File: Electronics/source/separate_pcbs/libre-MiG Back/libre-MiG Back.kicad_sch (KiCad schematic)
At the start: 7 parts, among them J17 Conn_01x06, J18 Conn_01x03, SW18 SKRHABE010, SW2 SW_Push, SW3 SW_Push

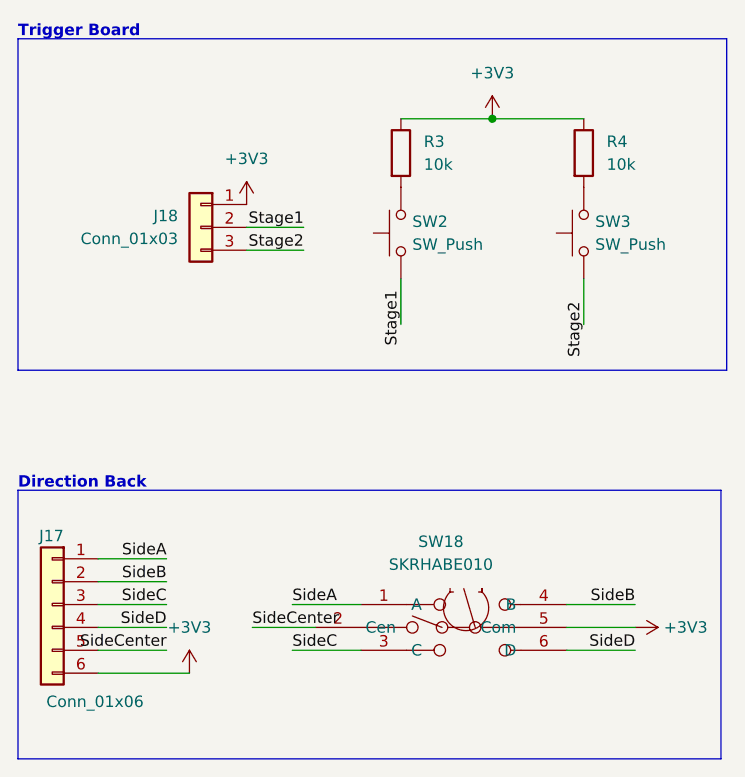
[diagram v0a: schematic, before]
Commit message: started layout and finished board shapes
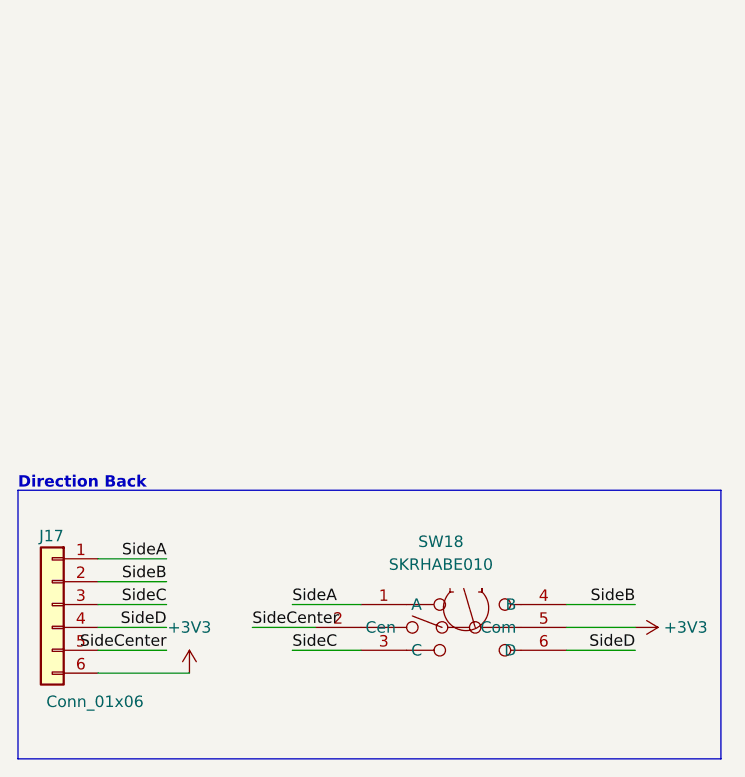
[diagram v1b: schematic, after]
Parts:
- removed J18: Conn_01x03, Connector_JST:JST_PH_S3B-PH-K_1x03_P2.00mm_Horizontal, symbol Connector_Generic:Conn_01x03
- removed R3, R4: 10k, Resistor_SMD:R_0805_2012Metric, symbol Device:R
- removed SW2, SW3: SW_Push, Button_Switch_THT:SW_PUSH-12mm_Wuerth-430476085716, symbol Switch:SW_Push
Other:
- note removed: "Trigger Board"
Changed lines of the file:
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@@
     (rev "v0.1")
-  )
-  (junction (at 111.76 57.15) (diameter 0) (color 0 0 0 0)
   )
   (wire (pts (xy 120.015 111.125) (xy 127.635 111.125))
@@
   )
   (wire (pts (xy 120.015 116.205) (xy 127.635 116.205))
-    (stroke (width 0) (type default) (color 0 0 0 0))
-  )
-  (wire (pts (xy 90.805 69.215) (xy 84.455 69.215))
     (stroke (width 0) (type default) (color 0 0 0 0))
   )
@@
     (stroke (width 0) (type default) (color 0 0 0 0))
   )
-  (polyline (pts (xy 59.055 48.26) (xy 137.795 48.26))
-    (stroke (width 0) (type default) (color 0 0 0 0))
-  )
-  (wire (pts (xy 90.805 71.755) (xy 84.455 71.755))
-    (stroke (width 0) (type default) (color 0 0 0 0))
-  )
-  (polyline (pts (xy 59.055 48.26) (xy 59.055 85.09))
-    (stroke (width 0) (type default) (color 0 0 0 0))
-  )
   (wire (pts (xy 75.565 108.585) (xy 67.945 108.585))
     (stroke (width 0) (type default) (color 0 0 0 0))
   )
-  (polyline (pts (xy 137.795 85.09) (xy 59.055 85.09))
-    (stroke (width 0) (type default) (color 0 0 0 0))
-  )
   (polyline (pts (xy 59.055 98.425) (xy 59.055 128.27))
-    (stroke (width 0) (type default) (color 0 0 0 0))
-  )
-  (wire (pts (xy 101.6 57.15) (xy 111.76 57.15))
-    (stroke (width 0) (type default) (color 0 0 0 0))
-  )
-  (wire (pts (xy 121.92 74.93) (xy 121.92 80.01))
-    (stroke (width 0) (type default) (color 0 0 0 0))
-  )
-  (polyline (pts (xy 137.795 48.26) (xy 137.795 85.09))
     (stroke (width 0) (type default) (color 0 0 0 0))
   )
@@
   )
   (wire (pts (xy 89.535 111.125) (xy 97.155 111.125))
-    (stroke (width 0) (type default) (color 0 0 0 0))
-  )
-  (wire (pts (xy 101.6 74.93) (xy 101.6 80.01))
     (stroke (width 0) (type default) (color 0 0 0 0))
   )
@@
     (stroke (width 0) (type default) (color 0 0 0 0))
   )
-  (wire (pts (xy 121.92 57.15) (xy 111.76 57.15))
-    (stroke (width 0) (type default) (color 0 0 0 0))
-  )
-  (text "Trigger Board" (at 59.055 48.26 0)
-    (effects (font (size 1.27 1.27) (thickness 0.254) bold) (justify left bottom))
-  )
   (text "Direction Back" (at 59.055 98.425 0)
     (effects (font (size 1.27 1.27) (thickness 0.254) bold) (justify left bottom))
   )
-  (label "Stage1" (at 101.6 76.2 270)
-    (effects (font (size 1.27 1.27)) (justify right bottom))
-  )
   (label "SideCenter" (at 75.565 116.205 180)
-    (effects (font (size 1.27 1.27)) (justify right bottom))
-  )
-  (label "Stage2" (at 90.805 71.755 180)
     (effects (font (size 1.27 1.27)) (justify right bottom))
   )
@@
     (effects (font (size 1.27 1.27)) (justify right bottom))
   )
-  (label "Stage2" (at 121.92 77.47 270)
-    (effects (font (size 1.27 1.27)) (justify right bottom))
-  )
-  (label "Stage1" (at 90.805 69.215 180)
-    (effects (font (size 1.27 1.27)) (justify right bottom))
-  )
   (label "SideD" (at 75.565 113.665 180)
     (effects (font (size 1.27 1.27)) (justify right bottom))
@@
   (label "SideD" (at 127.635 116.205 180)
     (effects (font (size 1.27 1.27)) (justify right bottom))
-  )
-  (symbol (lib_id "Switch:SW_Push") (at 121.92 69.85 90) (unit 1)
-    (in_bom yes) (on_board yes) (fields_autoplaced)
-    (property "Reference" "SW3" (id 0) (at 123.19 68.5799 90)
-      (effects (font (size 1.27 1.27)) (justify right))
-    )
-    (property "Value" "SW_Push" (id 1) (at 123.19 71.1199 90)
-      (effects (font (size 1.27 1.27)) (justify right))
-    )
-    (property "Footprint" "Button_Switch_THT:SW_PUSH-12mm_Wuerth-430476085716" (id 2) (at 116.84 69.85 0)
-      (effects (font (size 1.27 1.27)) hide)
-    )
-    (property "Datasheet" "~" (id 3) (at 116.84 69.85 0)
-      (effects (font (size 1.27 1.27)) hide)
-    )
-    (pin "1")
-    (pin "2")
   )
   (symbol (lib_id "power:+3V3") (at 127.635 113.665 270) (mirror x) (unit 1)
@@
     )
     (property "Datasheet" "" (id 3) (at 127.635 113.665 0)
-      (effects (font (size 1.27 1.27)) hide)
-    )
-    (pin "1")
-  )
-  (symbol (lib_id "power:+3V3") (at 111.76 57.15 0) (unit 1)
-    (in_bom yes) (on_board yes) (fields_autoplaced)
-    (property "Reference" "#PWR0159" (id 0) (at 111.76 60.96 0)
-      (effects (font (size 1.27 1.27)) hide)
-    )
-    (property "Value" "+3V3" (id 1) (at 111.76 52.07 0))
-    (property "Footprint" "" (id 2) (at 111.76 57.15 0)
-      (effects (font (size 1.27 1.27)) hide)
-    )
-    (property "Datasheet" "" (id 3) (at 111.76 57.15 0)
       (effects (font (size 1.27 1.27)) hide)
     )
@@
     (pin "6")
   )
-  (symbol (lib_id "Device:R") (at 101.6 60.96 0) (unit 1)
-    (in_bom yes) (on_board yes) (fields_autoplaced)
-    (property "Reference" "R3" (id 0) (at 104.14 59.6899 0)
-      (effects (font (size 1.27 1.27)) (justify left))
-    )
-    (property "Value" "10k" (id 1) (at 104.14 62.2299 0)
-      (effects (font (size 1.27 1.27)) (justify left))
-    )
-    (property "Footprint" "Resistor_SMD:R_0805_2012Metric" (id 2) (at 99.822 60.96 90)
-      (effects (font (size 1.27 1.27)) hide)
-    )
-    (property "Datasheet" "~" (id 3) (at 101.6 60.96 0)
-      (effects (font (size 1.27 1.27)) hide)
-    )
-    (pin "1")
-    (pin "2")
-  )
   (symbol (lib_id "Personal:SKRHABE010") (at 109.855 113.665 0) (unit 1)
     (in_bom yes) (on_board yes) (fields_autoplaced)
@@
     (pin "6")
   )
-  (symbol (lib_id "Switch:SW_Push") (at 101.6 69.85 90) (unit 1)
-    (in_bom yes) (on_board yes) (fields_autoplaced)
-    (property "Reference" "SW2" (id 0) (at 102.87 68.5799 90)
-      (effects (font (size 1.27 1.27)) (justify right))
-    )
-    (property "Value" "SW_Push" (id 1) (at 102.87 71.1199 90)
-      (effects (font (size 1.27 1.27)) (justify right))
-    )
-    (property "Footprint" "Button_Switch_THT:SW_PUSH-12mm_Wuerth-430476085716" (id 2) (at 96.52 69.85 0)
-      (effects (font (size 1.27 1.27)) hide)
-    )
-    (property "Datasheet" "~" (id 3) (at 96.52 69.85 0)
-      (effects (font (size 1.27 1.27)) hide)
-    )
-    (pin "1")
-    (pin "2")
-  )
   (symbol (lib_id "power:+3V3") (at 78.105 118.745 0) (mirror y) (unit 1)
     (in_bom yes) (on_board yes) (fields_autoplaced)
@@
     (pin "1")
   )
-  (symbol (lib_id "power:+3V3") (at 84.455 66.675 0) (mirror y) (unit 1)
-    (in_bom yes) (on_board yes) (fields_autoplaced)
-    (property "Reference" "#PWR0158" (id 0) (at 84.455 70.485 0)
-      (effects (font (size 1.27 1.27)) hide)
+  (sheet_instances
+    (path "/" (page "1"))
+  )
+  (symbol_instances
+    (path "/3010db34-8a7d-4514-88eb-1fa756a192d5"
+      (reference "#PWR0111") (unit 1) (value "+3V3") (footprint "")
     )
-    (property "Value" "+3V3" (id 1) (at 84.455 61.595 0))
-    (property "Footprint" "" (id 2) (at 84.455 66.675 0)
-      (effects (font (size 1.27 1.27)) hide)
+    (path "/a4715f85-e290-4022-a732-387737b16cb4"
+      (reference "#PWR0197") (unit 1) (value "+3V3") (footprint "")
     )
-    (property "Datasheet" "" (id 3) (at 84.455 66.675 0)
-      (effects (font (size 1.27 1.27)) hide)
+    (path "/7451cdb8-ff3c-44d9-ab84-4e0d8ae748d9"
+      (reference "J17") (unit 1) (value "Conn_01x06") (footprint "Connector_JST:JST_PH_S6B-PH-K_1x06_P2.00mm_Horizontal")
     )
-    (pin "1")
-  )
-  (symbol (lib_id "Device:R") (at 121.92 60.96 0) (unit 1)
-    (in_bom yes) (on_board yes) (fields_autoplaced)
-    (property "Reference" "R4" (id 0) (at 124.46 59.6899 0)
-      (effects (font (size 1.27 1.27)) (justify left))
+    (path "/97b71919-58cf-4dbf-9750-0f7c07a727ac"
+      (reference "SW18") (unit 1) (value "SKRHABE010") (footprint "Personal:SKRHABE010")
     )
-    (property "Value" "10k" (id 1) (at 124.46 62.2299 0)
-      (effects (font (size 1.27 1.27)) (justify left))
-    )
-    (property "Footprint" "Resistor_SMD:R_0805_2012Metric" (id 2) (at 120.142 60.96 90)
-      (effects (font (size 1.27 1.27)) hide)
-    )
-    (property "Datasheet" "~" (id 3) (at 121.92 60.96 0)
-      (effects (font (size 1.27 1.27)) hide)
-    )
-    (pin "1")
-    (pin "2")
-  )
-  (symbol (lib_id "Connector_Generic:Conn_01x03") (at 79.375 69.215 0) (mirror y) (unit 1)
-    (in_bom yes) (on_board yes) (fields_autoplaced)
-    (property "Reference" "J18" (id 0) (at 76.835 67.9449 0)
-      (effects (font (size 1.27 1.27)) (justify left))
-    )
-    (property "Value" "Conn_01x03" (id 1) (at 76.835 70.4849 0)
-      (effects (font (size 1.27 1.27)) (justify left))
-    )
-    (property "Footprint" "Connector_JST:JST_PH_S3B-PH-K_1x03_P2.00mm_Horizontal" (id 2) (at 79.375 69.215 0)
-      (effects (font (size 1.27 1.27)) hide)
-    )
-    (property "Datasheet" "~" (id 3) (at 79.375 69.215 0)
-      (effects (font (size 1.27 1.27)) hide)
-    )
-    (pin "1")
-    (pin "2")
-    (pin "3")
   )
 )
